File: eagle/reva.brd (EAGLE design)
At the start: 160 x 100 mm, 220 parts, among them IC1 LM555D, IC2 74HC174D, SW1 SWITCH-BRUH

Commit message: Save board state
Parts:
- removed DF16: RGB_LED_XL, flashing_ece_2025:LED2727
- removed R76: (no value), adafruit:R0402
- removed SW1: SWITCH-BRUH, flashing_ece_2025:SW-K31391B
- added C6: 100n, adafruit:C0805
- added C7, C8, C9: 10u, adafruit:C0805
- added H1, H2, H3, H4: MOUNT-HOLE3.3, holes:3,3
- added J1: TYPE-C-31-M-12, TYPE-C-31-M-12:HRO_TYPE-C-31-M-12
- added L1: LQH3NPN2R2MJRL, LQH3NPN2R2MJRL:IND_LQH3NPN2R2MJRL
- added PWR: SWITCH-BRUH, flashing_ece_2025:SW-K31391B
- added R108: 100, adafruit:R0402
- added R109: 75k, adafruit:R0402
- added SJ1: (no value), jumper:SJ
- added U1: TPS63002DRCR, TPS63001DRCR:VREG_V62/16624-01YE
- C2: value 100n -> 10u; device adafruit:C0603 -> adafruit:C0805
- C4: value 4u7 -> 10u
- R1, R2: value (none) -> 470
- R96, R97: value 100k -> 75k
- moved BT1 710.9 mm to (16.0, 28.0), flipped to the bottom, turned to 270 degrees
- moved R101 697.1 mm to (29.0, -9.00)
- moved R102 697.1 mm to (29.0, -15.0)
- moved R103 697.1 mm to (29.0, -21.0)
- moved R104 697.1 mm to (29.0, -27.0)
- moved R105 697.1 mm to (29.0, -33.0)
- moved R106 697.1 mm to (29.0, -39.0)
- moved R107 697.1 mm to (29.0, -62.0)
- moved C1 521.8 mm to (96.0, -97.0)
- moved C3 521.8 mm to (96.0, -119.0)
- moved C4 521.8 mm to (96.0, -133.0)
- moved C5 521.8 mm to (96.0, -139.0)
- moved IC1 521.8 mm to (99.0, -62.0)
- moved IC2 521.8 mm to (102.0, -72.0)
- moved Q1 521.8 mm to (97.0, -80.0)
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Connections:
- net N$96 renamed TR
- net N$99 renamed CV
- removed net N$76: DF16.4, DF16.5, DF16.6, R76.1
- removed net N$97: IC1.7, R96.1, R97.2
- new net 5VBUCK: C2.1, C8.1, C9.1, SJ1.1, U1.1, U1.10
- new net BUCK_IN: C7.1, PWR.COM, R108.2, U1.5
- new net DIS: IC1.7, R109.2, R96.1, R97.2
- new net N$100: L1.1, U1.4
- new net N$101: L1.2, U1.2
- new net N$103: J1.A4_B9, J1.B4_A9, PWR.L
- new net N$104: BT1.P, BT1.P1, PWR.R
- new net VINA: C6.1, R108.1, U1.6, U1.7, U1.8
- net +5V: now also SJ1.2; no longer C2.1, R76.2
- net CLK_1HZ: now also IC2.9
- net GND: now also BT1.N, C6.2, C7.2, C8.2, C9.2, J1.A1_B12, J1.B1_A12, U1.11, U1.3, U1.9
- net N$98: now also R109.1
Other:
- board size 160 x 100 mm -> 85 x 55 mm

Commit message: Finish rough layout
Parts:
- C6: device adafruit:C0805 -> adafruit:C0603
- moved R18 338.5 mm to (80.0, 49.0), turned to 90 degrees
- moved R17 334.0 mm to (78.0, 49.0), turned to 90 degrees
- moved R16 329.0 mm to (75.0, 49.0), turned to 90 degrees
- moved R15 323.2 mm to (70.5, 49.0), turned to 90 degrees
- moved R14 317.5 mm to (66.0, 49.0), turned to 90 degrees
- moved R21 312.4 mm to (16.5, 40.5), flipped to the bottom, turned to 90 degrees
- moved R13 311.7 mm to (61.5, 49.0), turned to 90 degrees
- moved R20 308.9 mm to (5.50, 45.0), turned to 90 degrees
- moved R12 306.0 mm to (57.0, 49.0), turned to 90 degrees
- moved R19 304.3 mm to (3.00, 45.0), turned to 90 degrees
- moved R11 300.2 mm to (52.5, 49.0), turned to 90 degrees
- moved R10 294.5 mm to (48.0, 49.0), turned to 90 degrees
- moved R9 288.8 mm to (43.5, 49.0), turned to 90 degrees
- moved R8 283.0 mm to (39.0, 49.0), turned to 90 degrees
- moved R7 277.4 mm to (34.5, 49.0), turned to 90 degrees
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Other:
- board size 85 x 55 mm -> 89 x 55 mm
- board text added: "Congrats Grad!"
- board text added: "JLCJLCJLCJLC"

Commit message: Make first prototype board
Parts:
- moved R100 4.39 mm to (45.9, 9.20), turned to 0 degrees
- moved QB 2.08 mm to (47.7, 12.3)
- moved R104 1.30 mm to (27.5, 3.70)
- moved QG 1.20 mm to (41.4, 12.3)
- moved R99 1.10 mm to (40.0, 12.4)
- moved R29 0.91 mm to (74.6, 41.9)
- moved C5 0.50 mm to (11.5, 6.50)
- moved C3 0.30 mm to (9.00, 14.2)
- moved R98 0.30 mm to (33.5, 12.2)
- moved R48 0.30 mm to (44.3, 34.0)
- moved Q4 0.20 mm to (33.0, 4.20)
- moved Q5 0.20 mm to (37.0, 4.20)
- moved Q6 0.20 mm to (41.0, 4.20)
- moved R107 0.10 mm to (46.0, 6.90)
- moved R109 0.10 mm to (15.9, 10.5), flipped to the bottom
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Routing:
- net +5V: track 0.00 -> 783.5 mm, vias 0 -> 29
- net G-: track 0.00 -> 531.4 mm, vias 0 -> 18
- net B-: track 0.00 -> 422.0 mm, vias 0 -> 24
- net R-: track 0.00 -> 367.3 mm, vias 0 -> 26
- net N$104: track 0.00 -> 63.4 mm
- net GND: track 0.00 -> 38.8 mm, vias 3 -> 31
- net DIN: track 0.00 -> 34.8 mm, vias 0 -> 1
- net FFQ3: track 0.00 -> 27.9 mm, vias 0 -> 1
- net Q6B: track 0.00 -> 25.0 mm, vias 0 -> 2
- net Q3B: track 0.00 -> 19.0 mm, vias 0 -> 2
- net FFQ2: track 0.00 -> 18.4 mm, vias 0 -> 1
- net CLK_1HZ: track 0.00 -> 18.4 mm, vias 0 -> 1
- net BUCK_IN: track 0.00 -> 18.3 mm, vias 0 -> 2
- net FFQ4: track 0.00 -> 18.0 mm, vias 0 -> 2
- net Q5B: track 0.00 -> 16.5 mm
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- added copper zone on layer 1, net 5VBUCK
- added copper zone on layer 1, net BUCK_IN
- added copper zone on layer 1, net GND
- added copper zone on layer 2, net GND
- added copper zone on layer 1, net N$100
- added copper zone on layer 1, net N$101
- added copper zone on layer 1, net VINA
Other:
- board text added: "Designed by Will Buchta 4/2025"

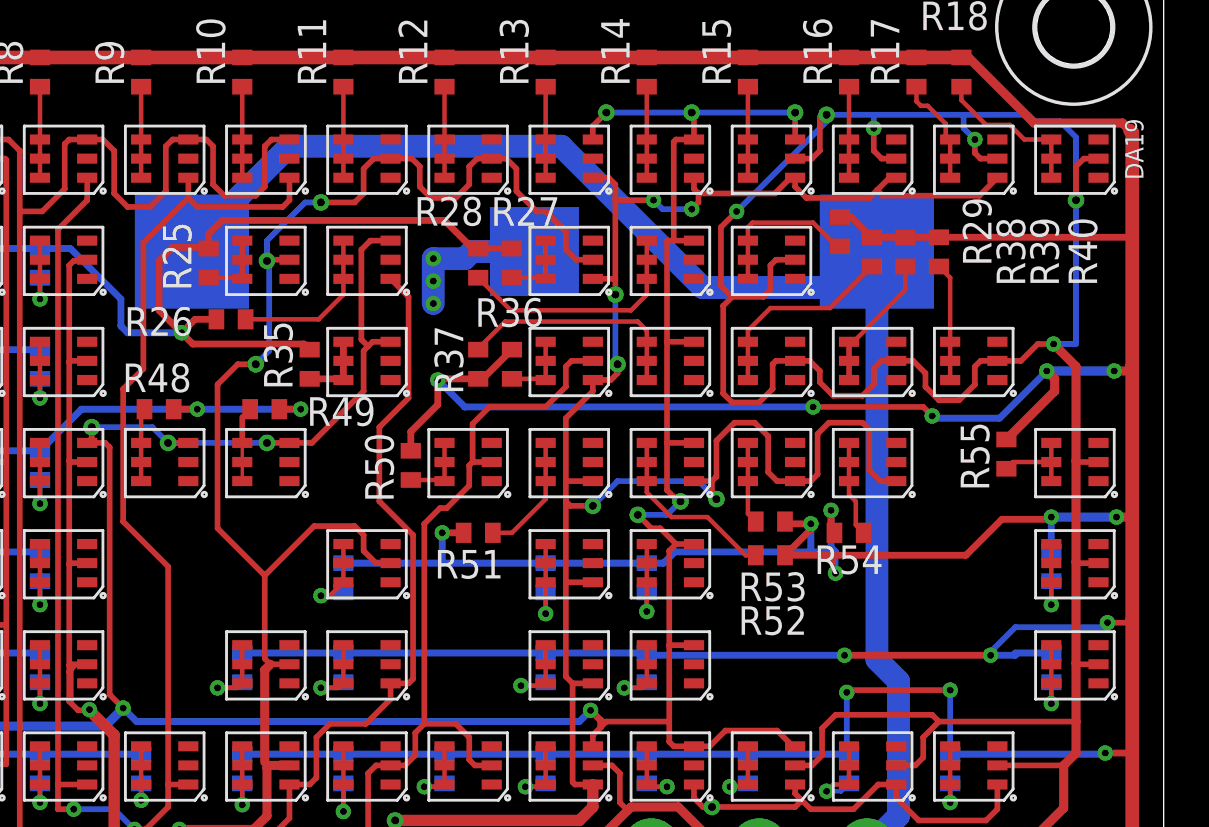
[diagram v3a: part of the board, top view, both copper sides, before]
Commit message: Change battery holder, create BOM and PNP
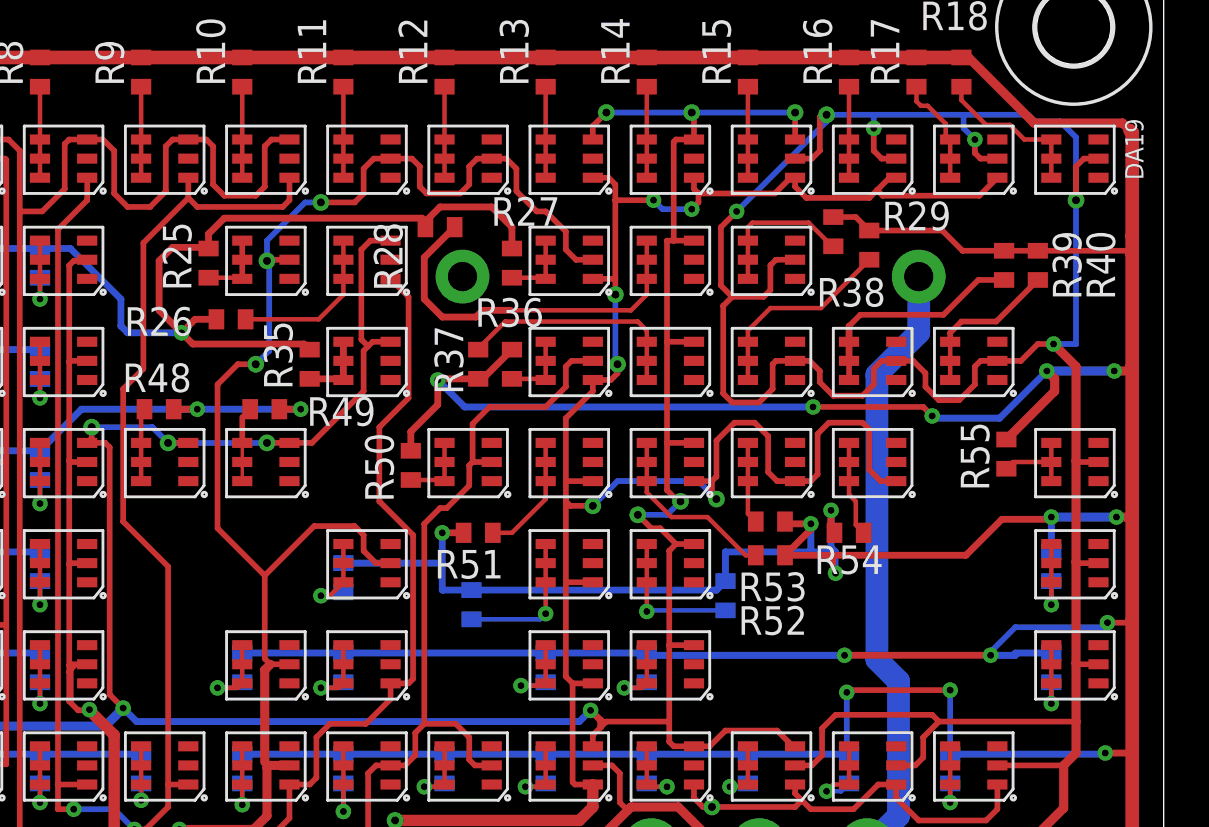
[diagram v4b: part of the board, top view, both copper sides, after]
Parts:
- removed BT1: 3P-3008-CR2450, Battery_Holder:BAT_3008
- added BAT1: CR2450, flashing_ece_2025:CR240_CASE
- moved R39 4.44 mm to (81.9, 40.4)
- moved R40 4.44 mm to (83.4, 40.4)
- moved R64 3.59 mm to (69.5, 25.7)
- moved R63 3.51 mm to (58.2, 25.3)
- moved R28 2.33 mm to (56.8, 42.1), turned to 180 degrees
- moved R38 0.32 mm to (75.9, 41.3)
- moved R29 0.30 mm to (74.3, 41.9)
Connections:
- net GND: now also BAT1.NEG; no longer BT1.N
- net N$104: now also BAT1.POS; no longer BT1.P, BT1.P1
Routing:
- net N$104: track 63.4 -> 27.1 mm
- net GND: track 38.8 -> 32.2 mm, vias 31 -> 28
- net N$28: track 10.8 -> 16.8 mm
- net +5V: track 783.5 -> 788.0 mm
- net N$39: track 6.24 -> 10.3 mm
- net N$64: track 3.85 -> 6.52 mm
- net N$63: track 4.05 -> 6.50 mm
- net N$40: track 5.26 -> 6.97 mm

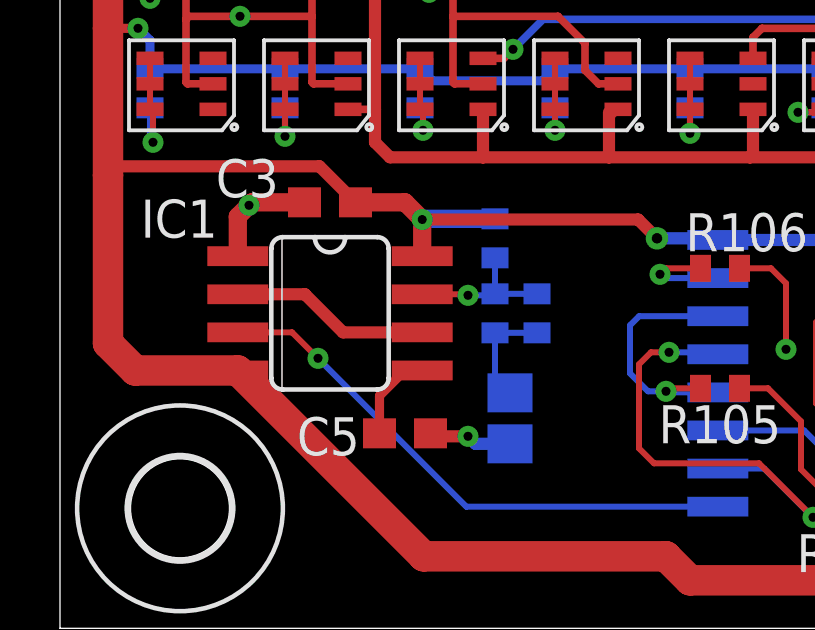
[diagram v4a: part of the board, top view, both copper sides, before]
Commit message: Fix 555 error
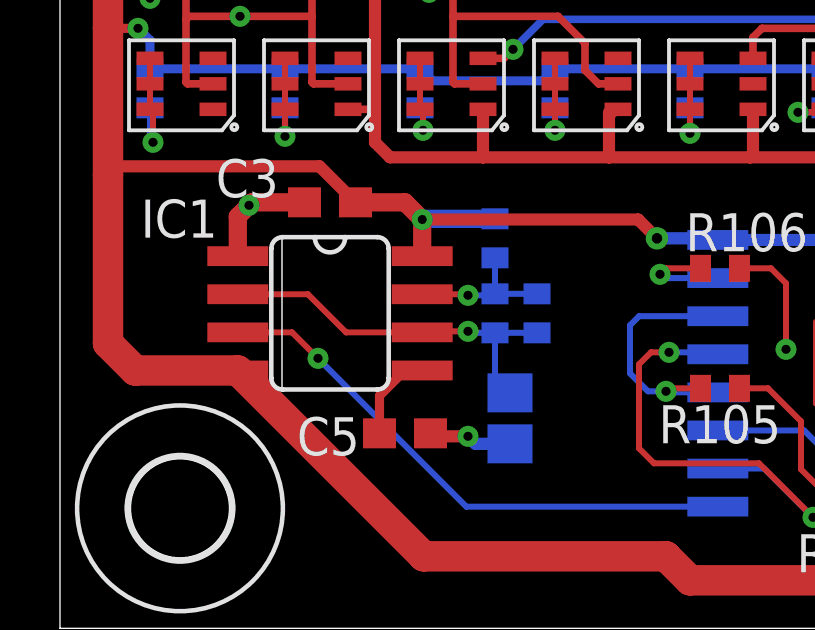
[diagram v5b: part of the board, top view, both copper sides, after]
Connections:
- removed net N$98: C4.1, R109.1, R97.1
- net TR: now also C4.1, R109.1, R97.1
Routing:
- net TR: track 6.67 -> 12.7 mm, vias 0 -> 1
- net N$98: track 3.61 -> 0.00 mm
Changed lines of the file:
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@@
 <layers>
 <layer number="1" name="Top" color="4" fill="1" visible="yes" active="yes"/>
-<layer number="2" name="Route2" color="16" fill="1" visible="no" active="yes"/>
+<layer number="2" name="Route2" color="16" fill="1" visible="yes" active="yes"/>
 <layer number="3" name="Route3" color="17" fill="1" visible="no" active="no"/>
 <layer number="4" name="Route4" color="18" fill="1" visible="no" active="no"/>
@@
 <layer number="13" name="Route13" color="21" fill="1" visible="no" active="no"/>
 <layer number="14" name="Route14" color="22" fill="1" visible="no" active="no"/>
-<layer number="15" name="Route15" color="23" fill="1" visible="no" active="yes"/>
-<layer number="16" name="Bottom" color="1" fill="1" visible="no" active="yes"/>
+<layer number="15" name="Route15" color="23" fill="1" visible="yes" active="yes"/>
+<layer number="16" name="Bottom" color="1" fill="1" visible="yes" active="yes"/>
 <layer number="17" name="Pads" color="2" fill="1" visible="yes" active="yes"/>
 <layer number="18" name="Vias" color="2" fill="1" visible="yes" active="yes"/>
@@
 <layer number="20" name="Dimension" color="24" fill="1" visible="yes" active="yes"/>
 <layer number="21" name="tPlace" color="7" fill="1" visible="yes" active="yes"/>
-<layer number="22" name="bPlace" color="7" fill="1" visible="no" active="yes"/>
+<layer number="22" name="bPlace" color="7" fill="1" visible="yes" active="yes"/>
 <layer number="23" name="tOrigins" color="15" fill="1" visible="yes" active="yes"/>
-<layer number="24" name="bOrigins" color="15" fill="1" visible="no" active="yes"/>
+<layer number="24" name="bOrigins" color="15" fill="1" visible="yes" active="yes"/>
 <layer number="25" name="tNames" color="7" fill="1" visible="yes" active="yes"/>
-<layer number="26" name="bNames" color="7" fill="1" visible="no" active="yes"/>
+<layer number="26" name="bNames" color="7" fill="1" visible="yes" active="yes"/>
 <layer number="27" name="tValues" color="7" fill="1" visible="no" active="yes"/>
 <layer number="28" name="bValues" color="7" fill="1" visible="no" active="yes"/>
@@
 <layer number="38" name="bTest" color="7" fill="1" visible="no" active="yes"/>
 <layer number="39" name="tKeepout" color="4" fill="11" visible="yes" active="yes"/>
-<layer number="40" name="bKeepout" color="1" fill="11" visible="no" active="yes"/>
+<layer number="40" name="bKeepout" color="1" fill="11" visible="yes" active="yes"/>
 <layer number="41" name="tRestrict" color="4" fill="10" visible="yes" active="yes"/>
-<layer number="42" name="bRestrict" color="1" fill="10" visible="no" active="yes"/>
+<layer number="42" name="bRestrict" color="1" fill="10" visible="yes" active="yes"/>
 <layer number="43" name="vRestrict" color="2" fill="10" visible="no" active="yes"/>
 <layer number="44" name="Drills" color="7" fill="1" visible="no" active="yes"/>
@@
 <layer number="50" name="dxf" color="7" fill="1" visible="no" active="yes"/>
 <layer number="51" name="tDocu" color="7" fill="1" visible="yes" active="yes"/>
-<layer number="52" name="bDocu" color="7" fill="1" visible="no" active="yes"/>
+<layer number="52" name="bDocu" color="7" fill="1" visible="yes" active="yes"/>
 <layer number="53" name="tGND_GNDA" color="7" fill="9" visible="no" active="no"/>
 <layer number="54" name="bGND_GNDA" color="1" fill="9" visible="no" active="no"/>
@@
 <contactref element="IC1" pad="2"/>
 <contactref element="IC1" pad="6"/>
-<wire x1="5.9266" y1="11.135" x2="8.165" y2="11.135" width="0.4064" layer="1"/>
-<wire x1="9.435" y1="9.865" x2="12.0734" y2="9.865" width="0.4064" layer="1"/>
-<wire x1="8.165" y1="11.135" x2="9.435" y2="9.865" width="0.4064" layer="1"/>
+<contactref element="C4" pad="1"/>
+<contactref element="R97" pad="1"/>
+<contactref element="R109" pad="1"/>
+<wire x1="15.9" y1="9.85" x2="14.5" y2="9.85" width="0.2" layer="16"/>
+<wire x1="15" y1="7.85" x2="14.5" y2="8.35" width="0.2" layer="16"/>
+<wire x1="14.5" y1="8.35" x2="14.5" y2="9.85" width="0.2" layer="16"/>
+<wire x1="5.9266" y1="11.135" x2="8.265" y2="11.135" width="0.2" layer="1"/>
+<wire x1="9.535" y1="9.865" x2="12.0734" y2="9.865" width="0.2" layer="1"/>
+<wire x1="8.265" y1="11.135" x2="9.535" y2="9.865" width="0.2" layer="1"/>
+<wire x1="14.5" y1="9.85" x2="13.65" y2="9.85" width="0.2" layer="16"/>
+<wire x1="13.65" y1="9.85" x2="13.6" y2="9.9" width="0.2" layer="16"/>
+<via x="13.6" y="9.9" extent="1-16" drill="0.3"/>
+<wire x1="13.6" y1="9.9" x2="12.1084" y2="9.9" width="0.2" layer="1"/>
+<wire x1="12.1084" y1="9.9" x2="12.0734" y2="9.865" width="0.2" layer="1"/>
 </signal>
 <signal name="DIS">
@@
 <wire x1="14.45" y1="11.1" x2="14.5" y2="11.15" width="0.2" layer="16"/>
 </signal>
-<signal name="N$98">
-<contactref element="C4" pad="1"/>
-<contactref element="R97" pad="1"/>
-<contactref element="R109" pad="1"/>
-<wire x1="15.9" y1="9.85" x2="14.5" y2="9.85" width="0.2" layer="16"/>
-<wire x1="15" y1="7.85" x2="14.5" y2="8.35" width="0.2" layer="16"/>
-<wire x1="14.5" y1="8.35" x2="14.5" y2="9.85" width="0.2" layer="16"/>
-</signal>
 <signal name="CV">
